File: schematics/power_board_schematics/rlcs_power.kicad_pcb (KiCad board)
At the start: 2 copper layers, 55.9 x 106.7 mm, 51 parts, among them J1 SD_Card, J10 Conn_14_to_21, J11 conn_power, J12 conn_A8_to_A15, J13 conn_A0_to_A7, J14 conn_22_to_53, J2 Conn_01x05_Male, J3 Conn_01x05_Male, J4 Battery Conn, J5 CONN_01X02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

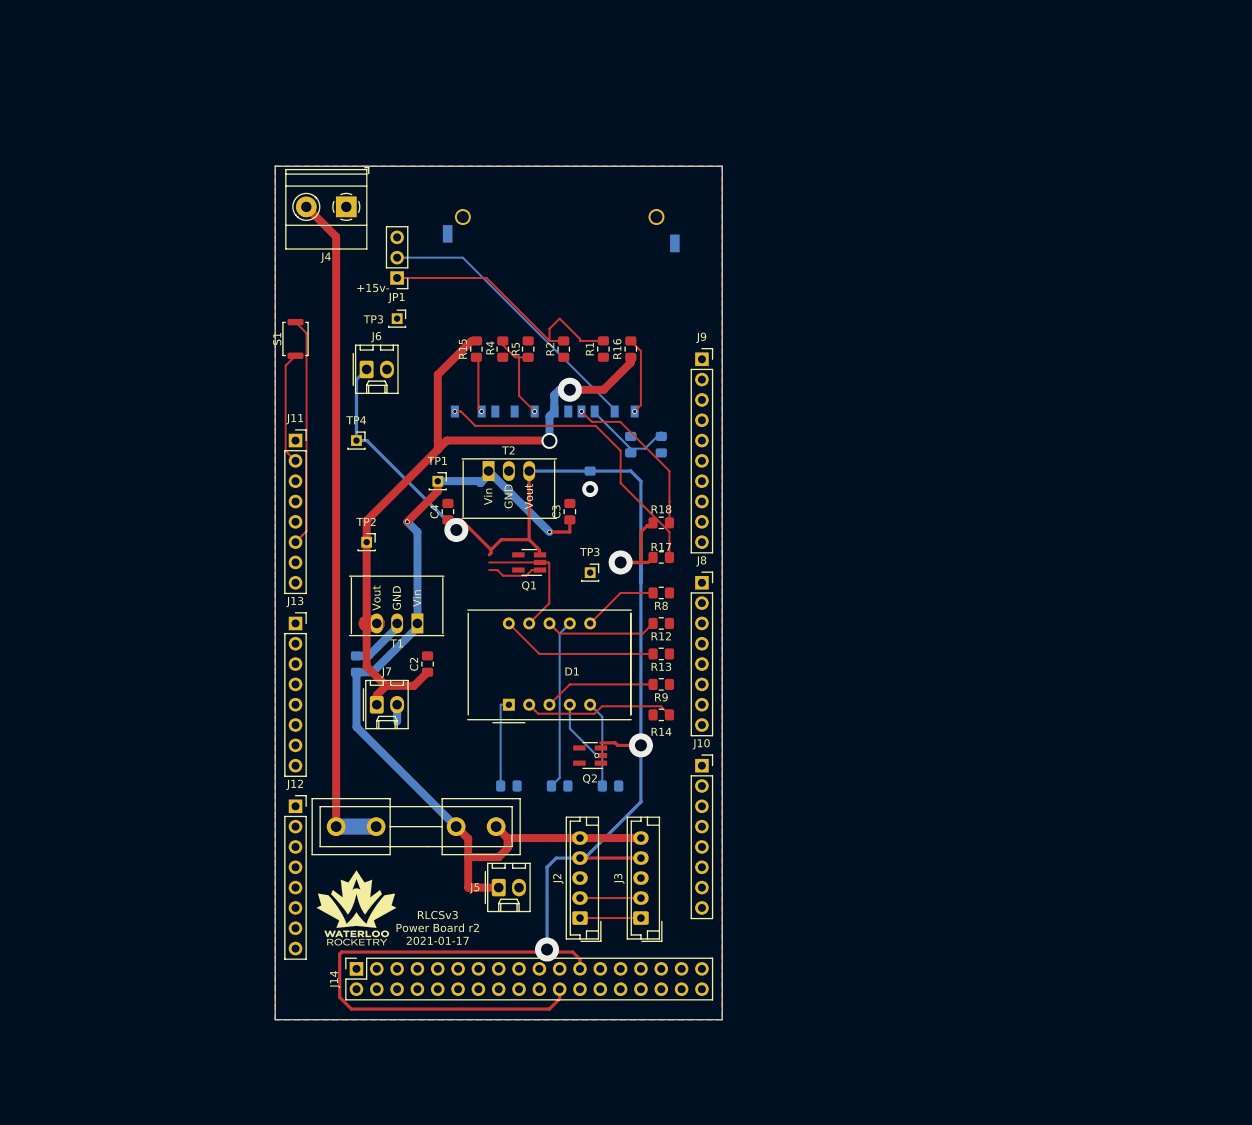
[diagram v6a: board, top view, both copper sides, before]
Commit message: Fix 7 segement display pins to make routing easier and fix footprints
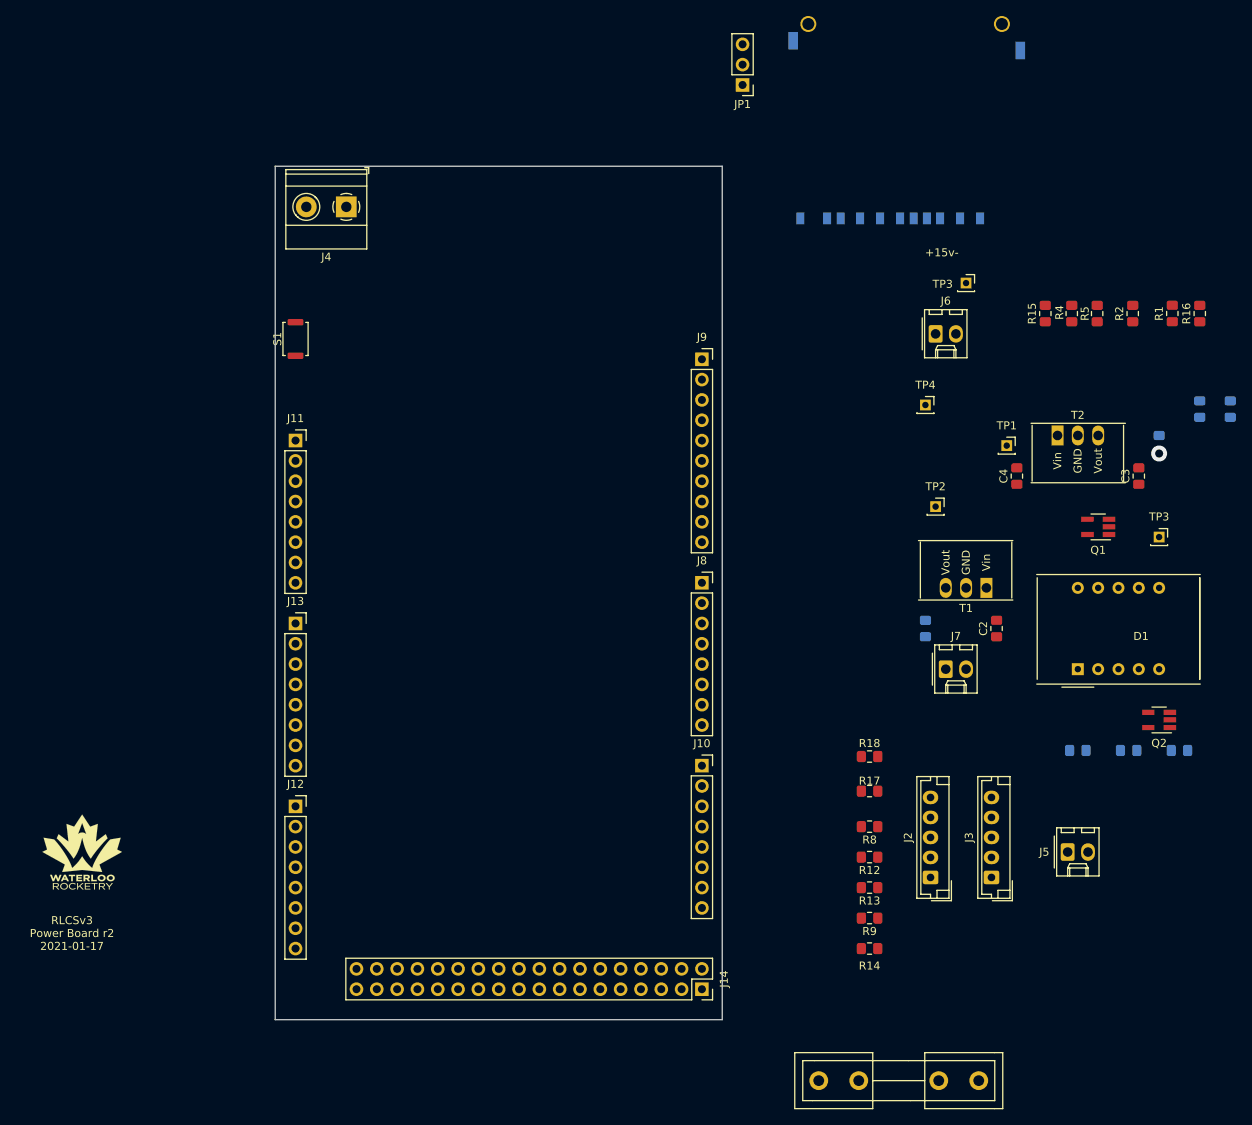
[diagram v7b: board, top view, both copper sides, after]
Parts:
- moved Q1 71.3 mm to (195.6, 106.0)
- moved T1 71.3 mm to (181.6, 113.7)
- moved C1 71.3 mm to (174.0, 118.7)
- moved C3 71.3 mm to (200.7, 99.7)
- moved J5 71.3 mm to (191.8, 146.7)
- moved J7 71.3 mm to (176.5, 123.8)
- moved R1 71.3 mm to (204.9, 79.4)
- moved R10 71.3 mm to (205.7, 134.0)
- moved R15 71.3 mm to (189.0, 79.4)
- moved R16 71.3 mm to (208.3, 79.4)
- moved R2 71.3 mm to (199.9, 79.4)
- moved R3 71.3 mm to (208.3, 91.3)
- moved R5 71.3 mm to (195.5, 79.4)
- moved R6 71.3 mm to (212.1, 91.3)
- moved T2 71.3 mm to (190.5, 94.6)
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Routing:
- net +5V: track 224.9 -> 0.00 mm, vias 4 -> 0
- net +12V: track 114.4 -> 0.00 mm, vias 2 -> 0
- net +3V3: track 94.1 -> 0.00 mm, vias 2 -> 0
- net Net-(F1-Pad1): track 84.0 -> 0.00 mm
- net ARD_CON_SD_WP: track 39.3 -> 0.00 mm, vias 1 -> 0
- net Net-(J1-Pad1): track 35.3 -> 0.00 mm
- net Net-(JP1-Pad1): track 34.2 -> 0.00 mm
- net Net-(J11-Pad6): track 28.6 -> 0.00 mm
- net Net-(AFF1-Pad7): track 21.3 -> 0.00 mm
- net ARD_CON_SD_CD: track 20.6 -> 0.00 mm, vias 1 -> 0
- net Net-(AFF1-Pad10): track 19.6 -> 0.00 mm
- net Net-(AFF1-Pad2): track 18.8 -> 0.00 mm
- net Net-(AFF1-Pad9): track 16.1 -> 0.00 mm
- net Net-(J11-Pad2): track 14.2 -> 0.00 mm
- net Net-(AFF1-Pad3): track 14.0 -> 0.00 mm
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- removed copper zone on B.Cu, net GND
- removed copper zone on F.Cu, net GND

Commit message: Update component placement
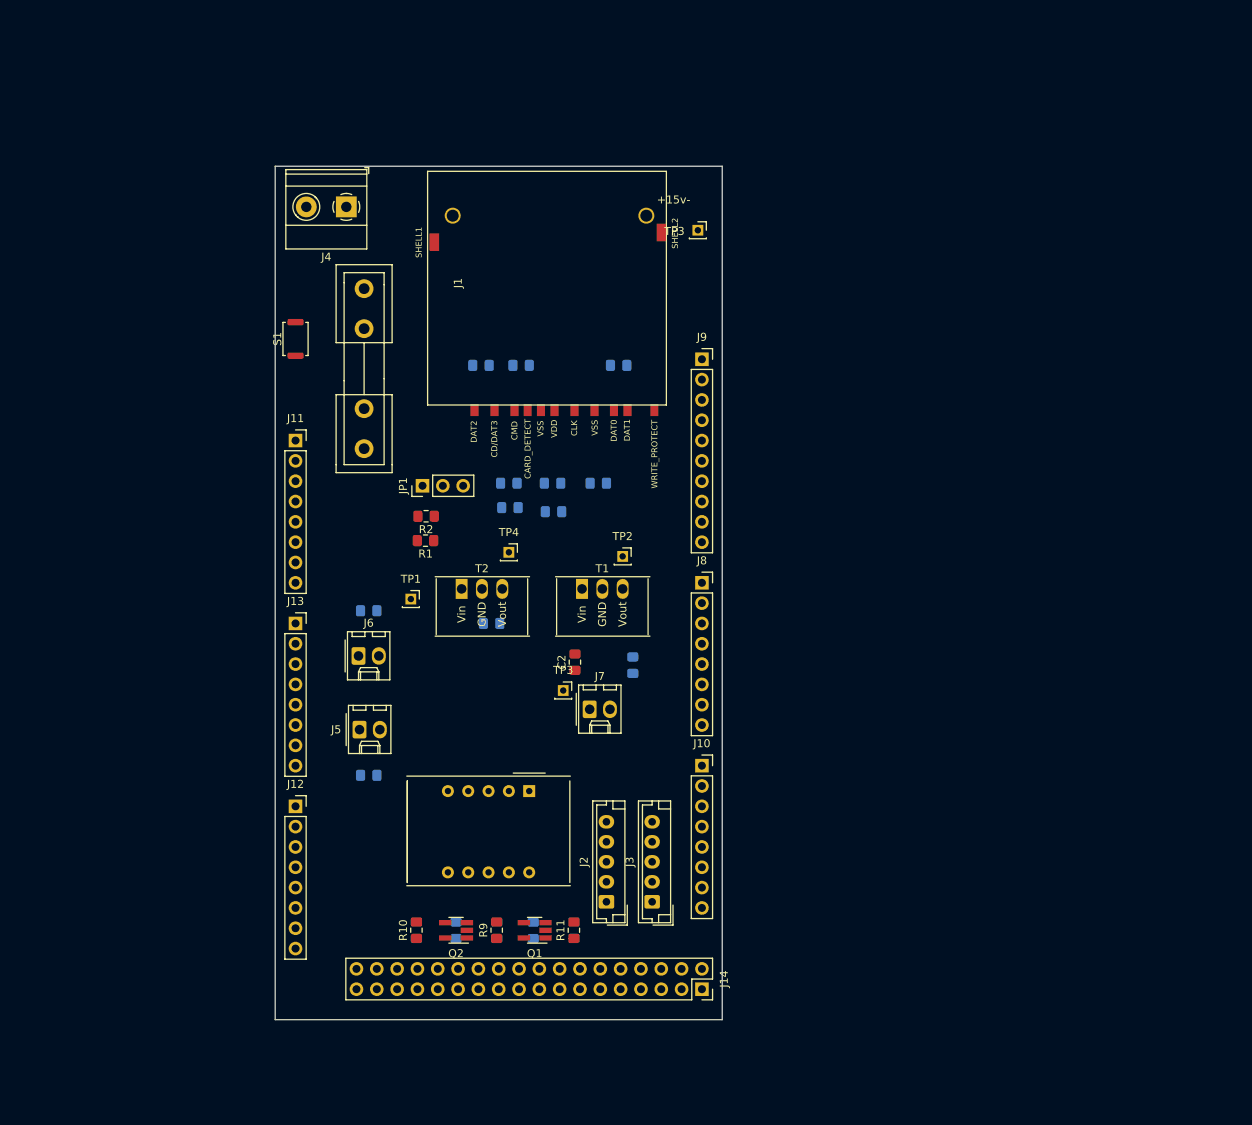
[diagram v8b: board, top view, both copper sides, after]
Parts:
- C3, C4, G***, R12, R13, R14, R15, R16, R17, R18, R4, R5, R8: moved to B.Cu
- J1, R10, R11: moved to F.Cu
- moved F1 114.2 mm to (103.8, 76.3), turned to 270 degrees
- moved C3 103.3 mm to (104.4, 137.1), turned to 0 degrees
- moved R10 98.0 mm to (110.4, 156.5), turned to 90 degrees
- moved R1 97.6 mm to (111.5, 107.8), turned to 0 degrees
- moved G*** 95.1 mm to (126.6, 71.3), turned to 180 degrees
- moved R2 91.9 mm to (111.6, 104.7), turned to 180 degrees
- moved Q2 91.7 mm to (115.3, 156.5)
- moved R6 90.7 mm to (121.9, 100.6), turned to 180 degrees
- moved R16 90.1 mm to (118.4, 85.9), turned to 180 degrees
- moved J5 89.8 mm to (103.3, 131.4)
- moved R3 87.1 mm to (122.0, 103.6), turned to 180 degrees
- moved R7 87.0 mm to (115.3, 156.5), turned to 90 degrees
- moved Q1 86.6 mm to (125.1, 156.5)
- moved C4 86.4 mm to (119.8, 118.1), turned to 180 degrees
- moved C4 82.7 mm to (104.4, 116.5), turned to 0 degrees
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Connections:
- J10 pad 20: Net-(J10-Pad20) -> ARD_CON_SDA
- J14 pad 34: Net-(J14-Pad34) -> ARD_CON_SD_CD
- J14 pad 35: Net-(J14-Pad35) -> ARD_CON_SD_WP
- J14 pad 40: Sevenseg_DP -> Sevenseg_D2
- J14 pad 41: Sevenseg_D2 -> Sevenseg_DP
- J14 pad 54: ARD_CON_SD_CD -> Net-(J14-Pad54)
- J14 pad 55: ARD_CON_SD_WP -> Net-(J14-Pad55)
- J2 pad 1: /SDA -> ARD_CON_SDA
- J2 pad 2: /SCL -> ARD_CON_SD_SCL
- J3 pad 1: /SDA -> ARD_CON_SDA
- J3 pad 2: /SCL -> ARD_CON_SD_SCL
- Q1 pad 1: ARD_CON_7SEG_D2 -> Sevenseg_D2
- Q2 pad 1: ARD_CON_7SEG_D1 -> Sevenseg_D1
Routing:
- net Sevenseg_C: track 0.00 -> 0.52 mm
- net GND: vias 1 -> 0
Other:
- board text removed: "CD/DAT3"
- board text removed: "CLK"
- board text removed: "CMD"
- board text removed: "D1"
- board text removed: "DAT0"
- board text removed: "DAT1"
- board text removed: "DAT2"
- board text removed: "VDD"
- board text removed: "VSS"
